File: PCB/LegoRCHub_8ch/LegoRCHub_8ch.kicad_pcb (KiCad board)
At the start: 2 copper layers, 39.3 x 55.2 mm, 39 parts, among them J1 Conn_01x02, J2 Conn_01x02, J3 Conn_01x02, J4 Conn_01x02, J5 Conn_01x02, J6 Conn_01x03, J7 Conn_01x03, J8 Conn_01x03, J9 Conn_01x02, U1 DRV8872DDA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

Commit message: LegoRCHub_8ch: working on pcb design...
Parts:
- C11, C12, C14, U6: moved to B.Cu
- C13: footprint Capacitor_SMD:C_1206_3216Metric_Pad1.33x1.80mm_HandSolder -> Capacitor_SMD:C_0603_1608Metric_Pad1.08x0.95mm_HandSolder; moved to B.Cu
- J1, J2, J3, J4, J5: footprint Connector_PinHeader_2.54mm:PinHeader_1x02_P2.54mm_Vertical -> Connector_PinHeader_2.54mm:PinHeader_1x02_P2.54mm_Vertical_SMD_Pin1Left; moved to F.Cu
- J6, J7, J8: footprint Connector_PinHeader_2.54mm:PinHeader_1x03_P2.54mm_Vertical -> Connector_PinHeader_2.54mm:PinHeader_1x03_P2.54mm_Vertical_SMD_Pin1Left; moved to F.Cu
- U7: value ATtiny1607-M -> ATtiny3226-X; footprint Package_DFN_QFN:QFN-24-1EP_4x4mm_P0.5mm_EP2.6x2.6mm -> Package_SO:SSOP-20_5.3x7.2mm_P0.65mm; moved to B.Cu
- moved R2 89.7 mm to (26.4, 50.8), turned to 90 degrees
- moved R1 85.5 mm to (26.4, 39.8), turned to 90 degrees
- moved U7 75.7 mm to (44.5, 44.8)
- moved C11 74.1 mm to (40.0, 61.8), turned to -90 degrees
- moved C13 68.9 mm to (44.5, 51.3), turned to 180 degrees
- moved C14 63.1 mm to (44.5, 49.8), turned to 180 degrees
- moved C12 56.5 mm to (40.0, 56.7), turned to 90 degrees
- moved R3 51.8 mm to (26.4, 61.8), turned to 90 degrees
- moved R5 49.8 mm to (62.5, 54.3), turned to 90 degrees
- moved R4 45.6 mm to (62.5, 43.3), turned to 90 degrees
- moved J9 44.0 mm to (44.5, 72.8), turned to 90 degrees
- moved U6 40.3 mm to (44.5, 59.3), turned to 90 degrees
- moved J7 32.6 mm to (49.5, 31.1), turned to -90 degrees
- moved J6 32.3 mm to (39.5, 31.1), turned to -90 degrees
- moved J8 6.06 mm to (54.5, 61.8), turned to -90 degrees
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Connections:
- C13 pad 2: +BATT -> VCC
- C14 pad 2: +BATT -> VCC
- U7 pad 1: unconnected-(U7-Pad1) -> VCC
- U7 pad 10: /CH4_2 -> /CH7_3
- U7 pad 11: /CH5_3 -> /CH8_3
- U7 pad 12: /CH5_2 -> /CH2_3
- U7 pad 13: /CH6_3 -> /CH2_2
- U7 pad 14: /CH7_3 -> /CH3_3
- U7 pad 15: /CH8_3 -> /CH3_2
- U7 pad 19: /CH2_3 -> /CH4_2
- U7 pad 2: unconnected-(U7-Pad2) -> /CH4_3
- U7 pad 20: /CH2_2 -> GND
- U7 pad 3: GND -> /CH5_2
- U7 pad 4: +BATT -> /CH5_3
- U7 pad 9: /CH4_3 -> /CH6_3
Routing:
- net VCC: track 0.00 -> 21.1 mm
- net /CH1_2: track 0.00 -> 19.0 mm, vias 0 -> 1
- net +BATT: track 0.00 -> 8.59 mm
- net (no net): track 0.00 -> 8.50 mm

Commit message: LegoRCHub_8ch: finished PCB (beta 1)
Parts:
- added J10: Conn_01x02, Connector_PinHeader_2.54mm:PinHeader_1x02_P2.54mm_Vertical, F.Cu at (49.2, 71.8)
- moved R4 5.30 mm to (60.7, 38.3), turned to 180 degrees
- moved R5 5.30 mm to (60.7, 49.3), turned to 180 degrees
- moved R1 3.35 mm to (27.9, 42.8), turned to 0 degrees
- moved R2 3.35 mm to (27.9, 53.8), turned to 0 degrees
- moved R3 3.35 mm to (27.9, 64.8), turned to 0 degrees
- moved J9 1.50 mm to (43.0, 72.8)
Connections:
- U7 pad 10: /CH7_3 -> /CH6_3
- U7 pad 11: /CH8_3 -> unconnected-(U7-Pad11)
- U7 pad 12: /CH2_3 -> /CH7_3
- U7 pad 13: /CH2_2 -> unconnected-(U7-Pad13)
- U7 pad 14: /CH3_3 -> /CH4_2
- U7 pad 15: /CH3_2 -> /CH4_3
- U7 pad 16: unconnected-(U7-Pad16) -> /UPDI
- U7 pad 17: /CH1_3 -> /CH5_2
- U7 pad 18: /CH1_2 -> /CH5_3
- U7 pad 19: /CH4_2 -> /CH8_3
- U7 pad 2: /CH4_3 -> /CH3_3
- U7 pad 3: /CH5_2 -> /CH3_2
- U7 pad 4: /CH5_3 -> /CH2_3
- U7 pad 5: unconnected-(U7-Pad5) -> /CH2_2
- U7 pad 6: unconnected-(U7-Pad6) -> /CH1_3
- U7 pad 7: unconnected-(U7-Pad7) -> /CH1_2
- U7 pad 9: /CH6_3 -> unconnected-(U7-Pad9)
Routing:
- net VCC: track 21.1 -> 139.5 mm, vias 0 -> 5
- net /CH1_3: track 0.00 -> 26.9 mm, vias 0 -> 1
- net /CH4_2: track 0.00 -> 26.8 mm, vias 0 -> 1
- net /UPDI: track 0.00 -> 26.5 mm
- net /CH3_3: track 0.00 -> 24.9 mm, vias 0 -> 1
- net /CH3_2: track 0.00 -> 24.9 mm, vias 0 -> 1
- net /CH4_3: track 0.00 -> 24.6 mm, vias 0 -> 1
- net /CH5_2: track 0.00 -> 20.0 mm, vias 0 -> 1
- net /CH2_3: track 0.00 -> 17.9 mm, vias 0 -> 1
- net /CH2_2: track 0.00 -> 17.7 mm, vias 0 -> 1
- net /CH5_3: track 0.00 -> 17.6 mm, vias 0 -> 1
- net /CH8_3: track 0.00 -> 15.5 mm, vias 0 -> 1
- net /CH7_3: track 0.00 -> 15.1 mm, vias 0 -> 1
- net /CH6_3: track 0.00 -> 14.2 mm, vias 0 -> 1
- net (no net): track 8.50 -> 0.00 mm
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
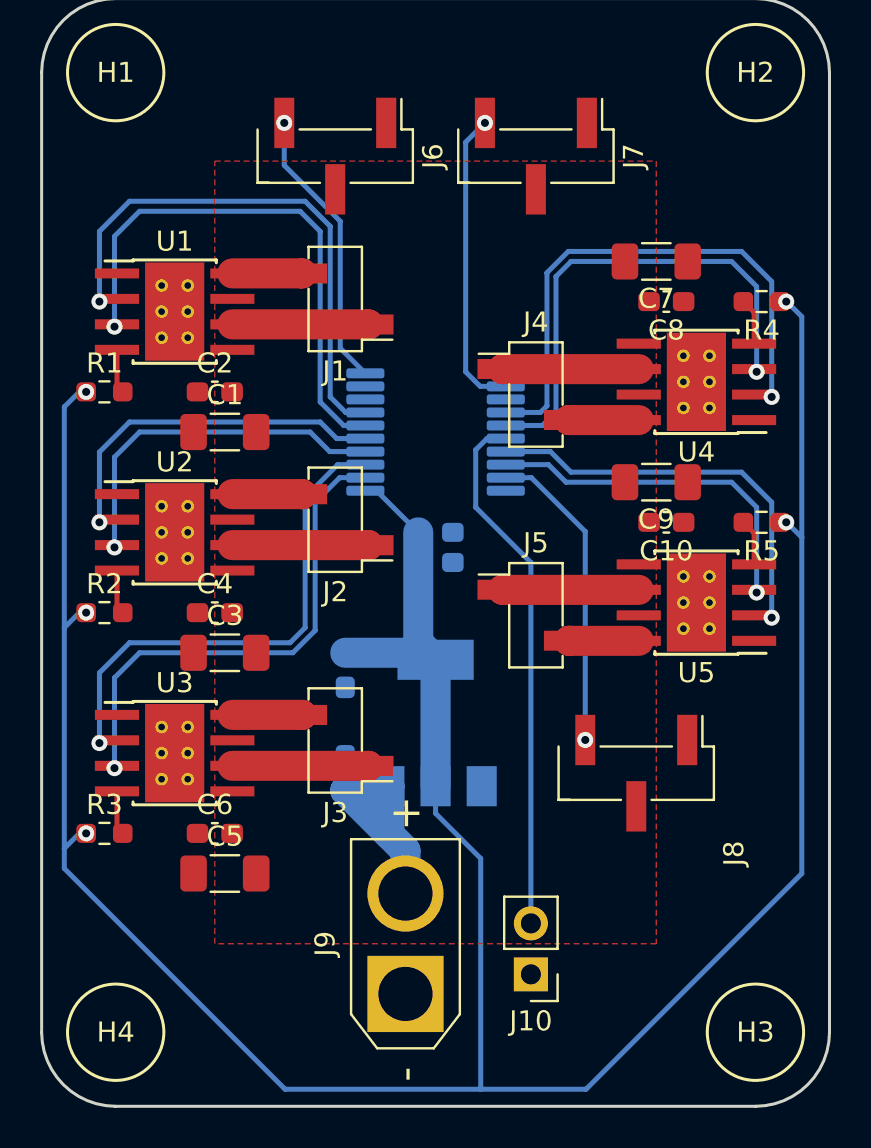
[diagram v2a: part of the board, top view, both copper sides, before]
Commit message: LegoRCHub_8ch: finished PCB (beta 2)
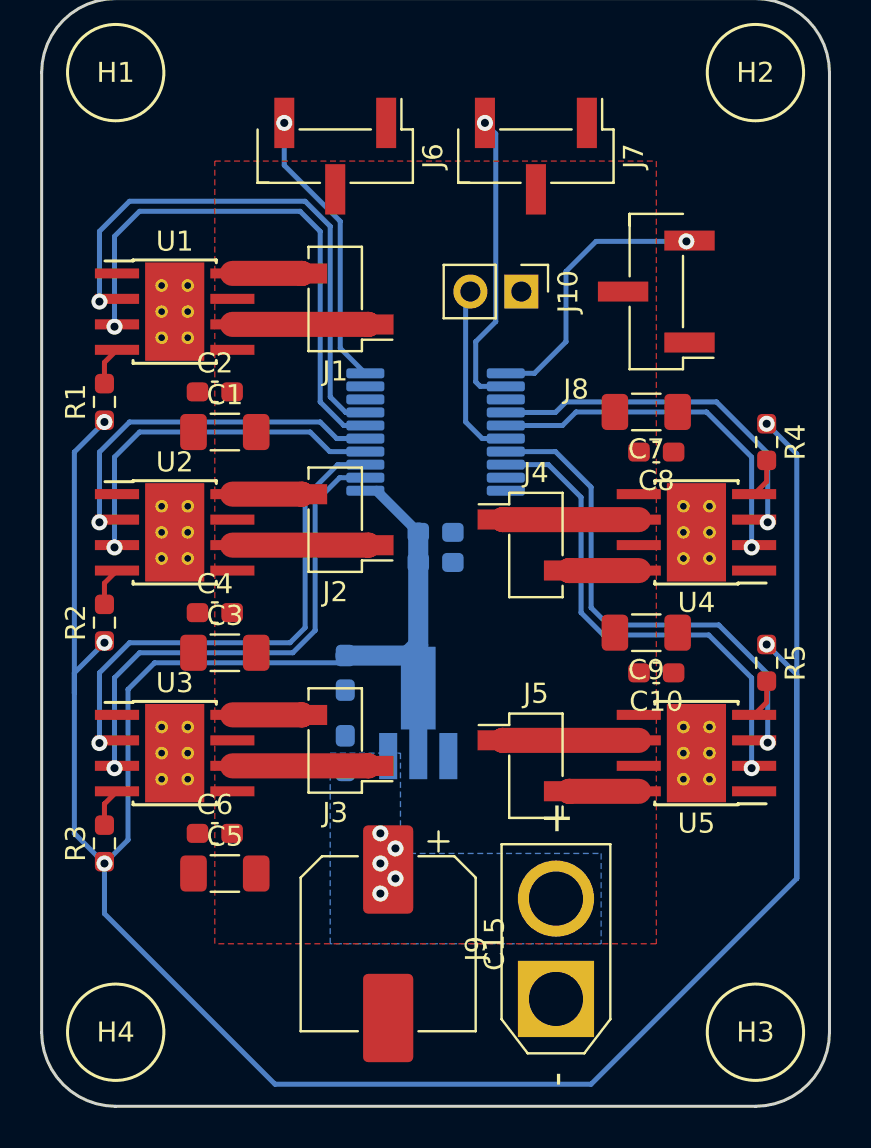
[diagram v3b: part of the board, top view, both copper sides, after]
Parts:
- added C15: 470uF, Capacitor_SMD:CP_Elec_8x10.5, F.Cu at (42.1, 70.3)
- U6: footprint Package_TO_SOT_SMD:SOT-223-3_TabPin2 -> Package_TO_SOT_SMD:SOT-89-3_Handsoldering
- moved J10 34.0 mm to (48.7, 37.8), turned to -90 degrees
- moved J8 24.0 mm to (55.5, 37.8), turned to 180 degrees
- moved C10 7.52 mm to (55.5, 56.8)
- moved C7 7.52 mm to (55.0, 43.8)
- moved C8 7.52 mm to (55.5, 45.8)
- moved C9 7.52 mm to (55.0, 54.8)
- moved J9 7.50 mm to (50.5, 73.0)
- moved J4 7.50 mm to (49.5, 50.4)
- moved J5 7.50 mm to (49.5, 61.4)
- moved U4 7.50 mm to (57.5, 49.8)
- moved U5 7.50 mm to (57.5, 60.8)
- moved R4 7.00 mm to (61.0, 45.3), turned to -90 degrees
- moved R5 7.00 mm to (61.0, 56.3), turned to -90 degrees
- moved C11 1.00 mm to (40.0, 60.8)
- moved U6 1.00 mm to (43.6, 58.8)
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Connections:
- U7 pad 11: unconnected-(U7-Pad11) -> /CH8_3
- U7 pad 14: /CH4_2 -> /CH4_3
- U7 pad 15: /CH4_3 -> /CH4_2
- U7 pad 17: /CH5_2 -> /CH5_3
- U7 pad 18: /CH5_3 -> /CH5_2
- U7 pad 19: /CH8_3 -> unconnected-(U7-Pad19)
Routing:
- net /UPDI: track 26.5 -> 8.61 mm
- net +BATT: track 11.1 -> 0.00 mm, vias 0 -> 5
- net /CH4_2: track 26.8 -> 18.0 mm
- net /CH5_3: track 17.6 -> 24.6 mm
- net /CH4_3: track 24.6 -> 17.8 mm
- net /CH5_2: track 20.0 -> 24.5 mm
- net /CH8_3: track 15.5 -> 13.8 mm
- added copper zone on B.Cu, net +BATT

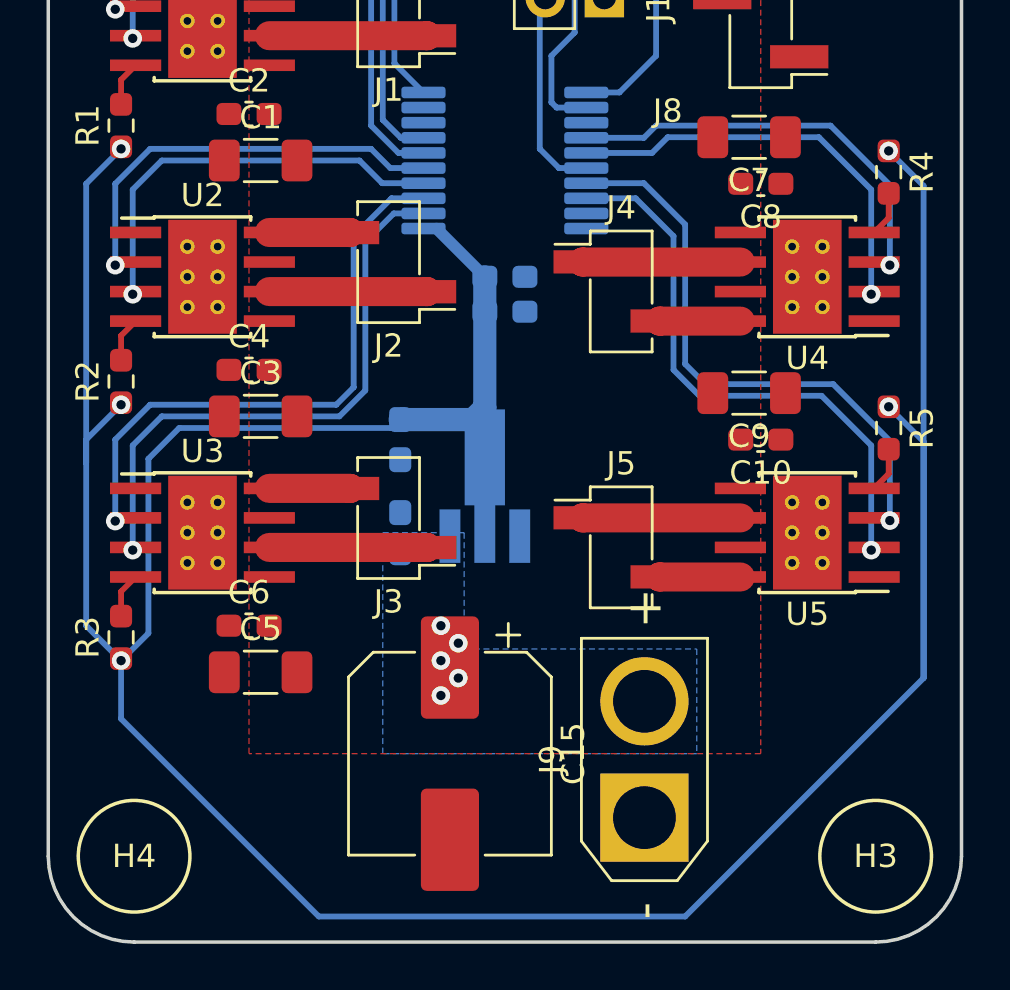
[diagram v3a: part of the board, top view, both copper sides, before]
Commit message: LegoRCHub_8ch: finished PCB (beta 3)
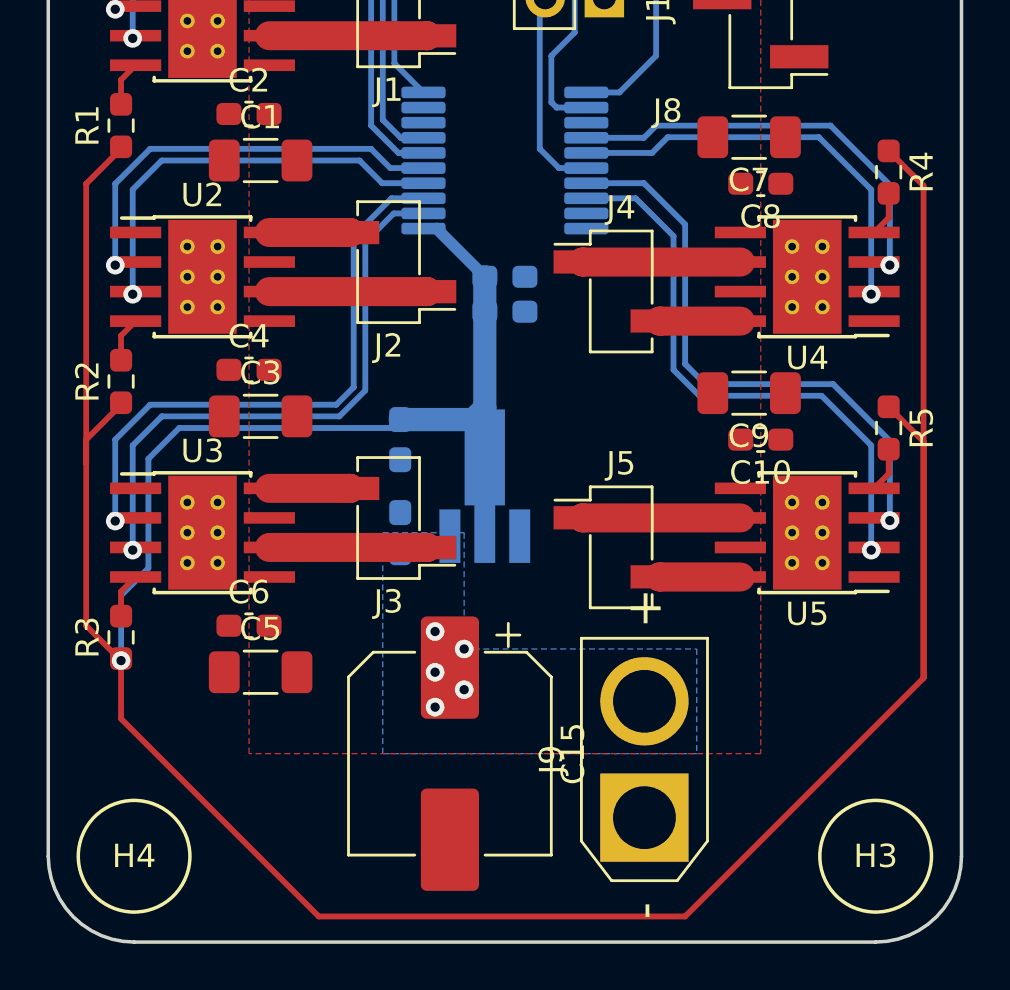
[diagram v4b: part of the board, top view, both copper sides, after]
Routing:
- net VCC: vias 5 -> 1
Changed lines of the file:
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@@
   (gr_line locked (start 64.08 74.71) (end 64.08 26.89) (layer "Edge.Cuts") (width 0.15))
   (gr_arc locked (start 24.82 26.89) (mid 25.900776 24.280776) (end 28.51 23.2) (layer "Edge.Cuts") (width 0.15))
-  (via (at 41.7 64.8) (size 0.8) (drill 0.4) (layers "F.Cu" "B.Cu") (net 2))
-  (via (at 42.45 67.05) (size 0.8) (drill 0.4) (layers "F.Cu" "B.Cu") (net 2))
-  (via (at 41.7 67.8) (size 0.8) (drill 0.4) (layers "F.Cu" "B.Cu") (net 2))
-  (via (at 41.7 66.3) (size 0.8) (drill 0.4) (layers "F.Cu" "B.Cu") (net 2))
-  (via (at 42.45 65.55) (size 0.8) (drill 0.4) (layers "F.Cu" "B.Cu") (net 2))
-  (via (at 60.95 55.3875) (size 0.8) (drill 0.4) (layers "F.Cu" "B.Cu") (net 3))
-  (via (at 27.95 44.3) (size 0.8) (drill 0.4) (layers "F.Cu" "B.Cu") (net 3))
+  (via (at 41.45 65.05) (size 0.8) (drill 0.4) (layers "F.Cu" "B.Cu") (net 2))
+  (via (at 42.7 67.55) (size 0.8) (drill 0.4) (layers "F.Cu" "B.Cu") (net 2))
+  (via (at 41.45 68.3) (size 0.8) (drill 0.4) (layers "F.Cu" "B.Cu") (net 2))
+  (via (at 41.45 66.8) (size 0.8) (drill 0.4) (layers "F.Cu" "B.Cu") (net 2))
+  (via (at 42.7 65.8) (size 0.8) (drill 0.4) (layers "F.Cu" "B.Cu") (net 2))
+  (segment (start 36.45 77.3) (end 52.2 77.3) (width 0.25) (layer "F.Cu") (net 3))
+  (segment (start 62.45 56.8875) (end 60.95 55.3875) (width 0.25) (layer "F.Cu") (net 3))
+  (segment (start 62.45 67.05) (end 62.45 45.8875) (width 0.25) (layer "F.Cu") (net 3))
+  (segment (start 27.95 66.3) (end 27.95 68.8) (width 0.25) (layer "F.Cu") (net 3))
+  (segment (start 62.45 45.8875) (end 60.95 44.3875) (width 0.25) (layer "F.Cu") (net 3))
+  (segment (start 27.95 44.3) (end 26.45 45.8) (width 0.25) (layer "F.Cu") (net 3))
+  (segment (start 27.95 55.3) (end 26.45 56.8) (width 0.25) (layer "F.Cu") (net 3))
+  (segment (start 26.45 45.8) (end 26.45 57.8) (width 0.25) (layer "F.Cu") (net 3))
+  (segment (start 26.45 56.8) (end 26.45 57.8) (width 0.25) (layer "F.Cu") (net 3))
+  (segment (start 26.45 64.8) (end 27.95 66.3) (width 0.25) (layer "F.Cu") (net 3))
+  (segment (start 52.2 77.3) (end 62.45 67.05) (width 0.25) (layer "F.Cu") (net 3))
+  (segment (start 26.45 57.8) (end 26.45 64.8) (width 0.25) (layer "F.Cu") (net 3))
+  (segment (start 62.45 67.05) (end 62.45 56.8875) (width 0.25) (layer "F.Cu") (net 3))
+  (segment (start 27.95 68.8) (end 36.45 77.3) (width 0.25) (layer "F.Cu") (net 3))
   (via (at 27.95 66.3) (size 0.8) (drill 0.4) (layers "F.Cu" "B.Cu") (net 3))
-  (via (at 60.95 44.3875) (size 0.8) (drill 0.4) (layers "F.Cu" "B.Cu") (net 3))
-  (via (at 27.95 55.3) (size 0.8) (drill 0.4) (layers "F.Cu" "B.Cu") (net 3))
-  (segment (start 36.45 77.3) (end 52.2 77.3) (width 0.25) (layer "B.Cu") (net 3))
+  (segment (start 27.95 66.3) (end 27.95 63.5) (width 0.25) (layer "B.Cu") (net 3))
   (segment (start 30.45 56.3) (end 39.5875 56.3) (width 0.25) (layer "B.Cu") (net 3))
-  (segment (start 27.95 66.3) (end 29.125 65.125) (width 0.25) (layer "B.Cu") (net 3))
   (segment (start 43.0875 55.9375) (end 43.5875 55.4375) (width 1) (layer "B.Cu") (net 3))
-  (segment (start 62.45 56.8875) (end 60.95 55.3875) (width 0.25) (layer "B.Cu") (net 3))
-  (segment (start 62.45 67.05) (end 62.45 45.8875) (width 0.25) (layer "B.Cu") (net 3))
-  (segment (start 27.95 66.3) (end 27.95 68.8) (width 0.25) (layer "B.Cu") (net 3))
-  (segment (start 62.45 45.8875) (end 60.95 44.3875) (width 0.25) (layer "B.Cu") (net 3))
-  (segment (start 27.95 44.3) (end 26.45 45.8) (width 0.25) (layer "B.Cu") (net 3))
   (segment (start 41.5125 47.725) (end 43.5875 49.8) (width 0.5) (layer "B.Cu") (net 3))
-  (segment (start 27.95 55.3) (end 26.45 56.8) (width 0.25) (layer "B.Cu") (net 3))
+  (segment (start 29.125 62.325) (end 29.125 57.625) (width 0.25) (layer "B.Cu") (net 3))
   (segment (start 39.5875 56.3) (end 39.95 55.9375) (width 0.25) (layer "B.Cu") (net 3))
-  (segment (start 26.45 45.8) (end 26.45 57.8) (width 0.25) (layer "B.Cu") (net 3))
-  (segment (start 26.45 56.8) (end 26.45 57.8) (width 0.25) (layer "B.Cu") (net 3))
   (segment (start 29.125 57.625) (end 30.45 56.3) (width 0.25) (layer "B.Cu") (net 3))
-  (segment (start 26.45 64.8) (end 27.95 66.3) (width 0.25) (layer "B.Cu") (net 3))
   (segment (start 43.5875 49.8) (end 43.5875 55.4375) (width 1) (layer "B.Cu") (net 3))
-  (segment (start 52.2 77.3) (end 62.45 67.05) (width 0.25) (layer "B.Cu") (net 3))
-  (segment (start 26.45 57.8) (end 26.45 64.8) (width 0.25) (layer "B.Cu") (net 3))
-  (segment (start 62.45 67.05) (end 62.45 56.8875) (width 0.25) (layer "B.Cu") (net 3))
-  (segment (start 29.125 65.125) (end 29.125 57.625) (width 0.25) (layer "B.Cu") (net 3))
+  (segment (start 27.95 63.5) (end 29.125 62.325) (width 0.25) (layer "B.Cu") (net 3))
   (segment (start 39.95 55.9375) (end 43.0875 55.9375) (width 1) (layer "B.Cu") (net 3))
-  (segment (start 27.95 68.8) (end 36.45 77.3) (width 0.25) (layer "B.Cu") (net 3))
   (segment (start 41.1 39.435) (end 41.105 39.44) (width 1.25) (layer "F.Cu") (net 4))
   (segment (start 34.325 39.435) (end 41.1 39.435) (width 1.25) (layer "F.Cu") (net 4))
@@
     (connect_pads yes (clearance 0.254))
     (min_thickness 0.254) (filled_areas_thickness no)
-    (fill yes (thermal_gap 0.508) (thermal_bridge_width 0.508) (smoothing fillet) (radius 1) (island_removal_mode 1) (island_area_min 0))
+    (fill yes (thermal_gap 0.508) (thermal_bridge_width 0.508) (smoothing fillet) (radius 2) (island_removal_mode 1) (island_area_min 0))
     (polygon
       (pts

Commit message: LegoRCHub_8ch_ServoVoltageConversion: working on pcb design...
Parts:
- added REF**: SOT-23-6, Package_TO_SOT_SMD:SOT-23-6, F.Cu at (75.2, 61.0)
- moved C13 28.0 mm to (72.5, 50.5)
- moved C14 28.0 mm to (72.5, 49.0)
- moved U7 28.0 mm to (72.5, 44.0)
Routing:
- net VCC: track 139.8 -> 111.1 mm, vias 1 -> 0
- net /CH1_3: track 26.9 -> 0.00 mm, vias 1 -> 0
- net /CH1_2: track 26.7 -> 0.00 mm, vias 1 -> 0
- net /CH3_3: track 24.9 -> 0.00 mm, vias 1 -> 0
- net /CH3_2: track 24.9 -> 0.00 mm, vias 1 -> 0
- net /CH5_3: track 24.6 -> 0.00 mm, vias 1 -> 0
- net /CH5_2: track 24.5 -> 0.00 mm, vias 1 -> 0
- net /CH4_2: track 18.0 -> 0.00 mm, vias 1 -> 0
- net /CH2_3: track 17.9 -> 0.00 mm, vias 1 -> 0
- net /CH4_3: track 17.8 -> 0.00 mm, vias 1 -> 0
- net /CH2_2: track 17.7 -> 0.00 mm, vias 1 -> 0
- net /CH7_3: track 15.1 -> 0.00 mm, vias 1 -> 0
- net /CH6_3: track 14.2 -> 0.00 mm, vias 1 -> 0
- net /CH8_3: track 13.8 -> 0.00 mm, vias 1 -> 0
- net /UPDI: track 8.61 -> 0.00 mm
